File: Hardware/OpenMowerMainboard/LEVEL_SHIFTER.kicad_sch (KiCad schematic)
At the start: 3 parts, among them Q13 BSS138

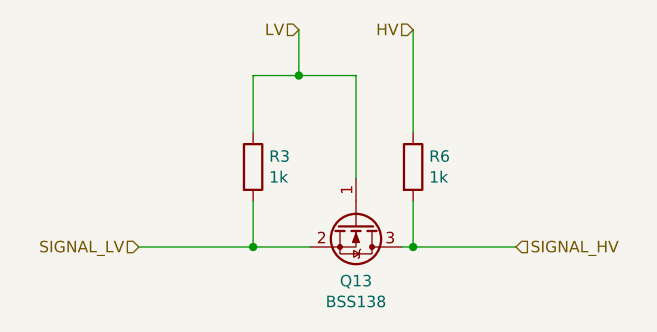
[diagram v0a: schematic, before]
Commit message: added todos, added image of current mainboard
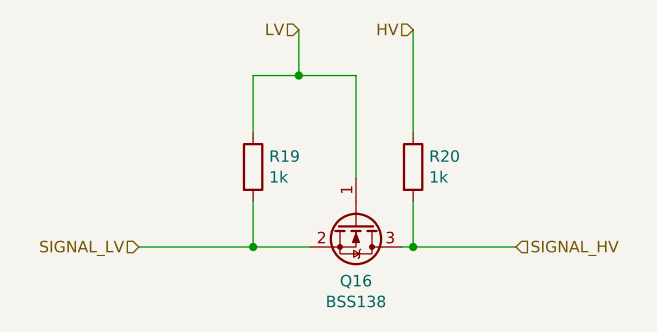
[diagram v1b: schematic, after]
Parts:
- renumbered Q13 to Q16, R3 to R19, R6 to R20
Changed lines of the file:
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@@
   (symbol (lib_id "Transistor_FET:BSS138") (at 114.3 76.2 270)
     (in_bom yes) (on_board yes)
-    (property "Reference" "Q13" (id 0) (at 114.3 82.5246 90))
+    (property "Reference" "Q16" (id 0) (at 114.3 82.5246 90))
     (property "Value" "BSS138" (id 1) (at 114.3 84.836 90))
     (property "Footprint" "Package_TO_SOT_SMD:SOT-23" (id 2) (at 112.395 81.28 0)
@@
   (symbol (lib_id "Device:R") (at 102.87 69.85 0)
     (in_bom yes) (on_board yes)
-    (property "Reference" "R3" (id 0) (at 104.648 68.6816 0)
+    (property "Reference" "R19" (id 0) (at 104.648 68.6816 0)
       (effects (font (size 1.27 1.27)) (justify left))
     )
@@
   (symbol (lib_id "Device:R") (at 120.65 69.85 0)
     (in_bom yes) (on_board yes)
-    (property "Reference" "R6" (id 0) (at 122.428 68.6816 0)
+    (property "Reference" "R20" (id 0) (at 122.428 68.6816 0)
       (effects (font (size 1.27 1.27)) (justify left))
     )

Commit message: BoM data added to kicad - results exported to .xlsx file
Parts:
- Q16: LCSC (none) -> C360338; Part Number (none) -> AP2300; Stock_PN (none) -> Q-AP2300
- R19, R20: Digikey (none) -> 311-1.00KCRCT-ND; Part Number (none) -> RC0805FR-071KL; Stock_PN (none) -> R-805-1K-.125W-1%
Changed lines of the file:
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@@
       (effects (font (size 1.27 1.27)) (justify left) hide)
+    )
+    (property "LCSC" "C360338" (id 4) (at 114.3 76.2 0)
+      (effects (font (size 1.27 1.27)) hide)
+    )
+    (property "Part Number" "AP2300" (id 5) (at 114.3 76.2 0)
+      (effects (font (size 1.27 1.27)) hide)
+    )
+    (property "Stock_PN" "Q-AP2300" (id 6) (at 114.3 76.2 0)
+      (effects (font (size 1.27 1.27)) hide)
     )
     (pin "1")
@@
       (effects (font (size 1.27 1.27)) hide)
     )
+    (property "Stock_PN" "R-805-1K-.125W-1%" (id 4) (at 102.87 69.85 0)
+      (effects (font (size 1.27 1.27)) hide)
+    )
+    (property "Digikey" "311-1.00KCRCT-ND" (id 5) (at 102.87 69.85 0)
+      (effects (font (size 1.27 1.27)) hide)
+    )
+    (property "Part Number" "RC0805FR-071KL" (id 6) (at 102.87 69.85 0)
+      (effects (font (size 1.27 1.27)) hide)
+    )
     (pin "1")
     (pin "2")
@@
       (effects (font (size 1.27 1.27)) hide)
     )
+    (property "Stock_PN" "R-805-1K-.125W-1%" (id 4) (at 120.65 69.85 0)
+      (effects (font (size 1.27 1.27)) hide)
+    )
+    (property "Digikey" "311-1.00KCRCT-ND" (id 5) (at 120.65 69.85 0)
+      (effects (font (size 1.27 1.27)) hide)
+    )
+    (property "Part Number" "RC0805FR-071KL" (id 6) (at 120.65 69.85 0)
+      (effects (font (size 1.27 1.27)) hide)
+    )
